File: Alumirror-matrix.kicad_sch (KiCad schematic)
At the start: 41 parts, among them K11 PG1350, K12 PG1350, K13 PG1350, K14 PG1350, K15 PG1350, K16 PG1350, K21 PG1350, K22 PG1350, K23 PG1350, K24 PG1350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

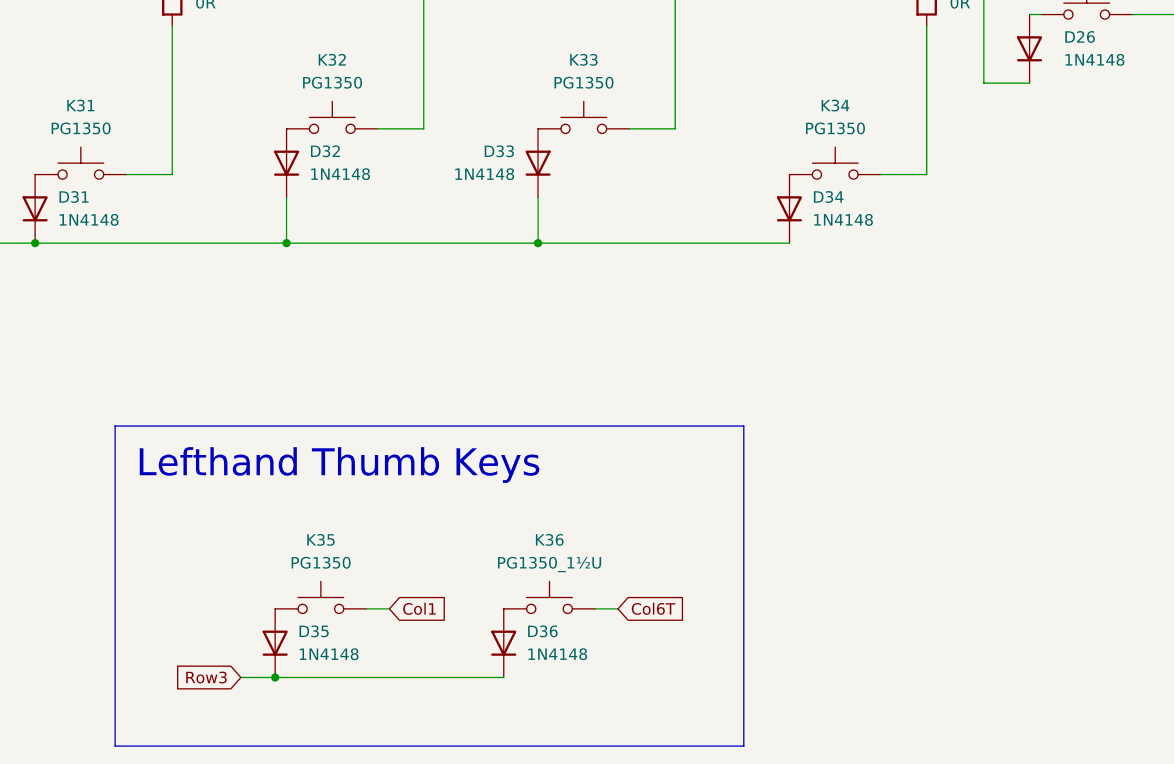
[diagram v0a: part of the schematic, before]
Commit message: Move thumb keys to new Row 4
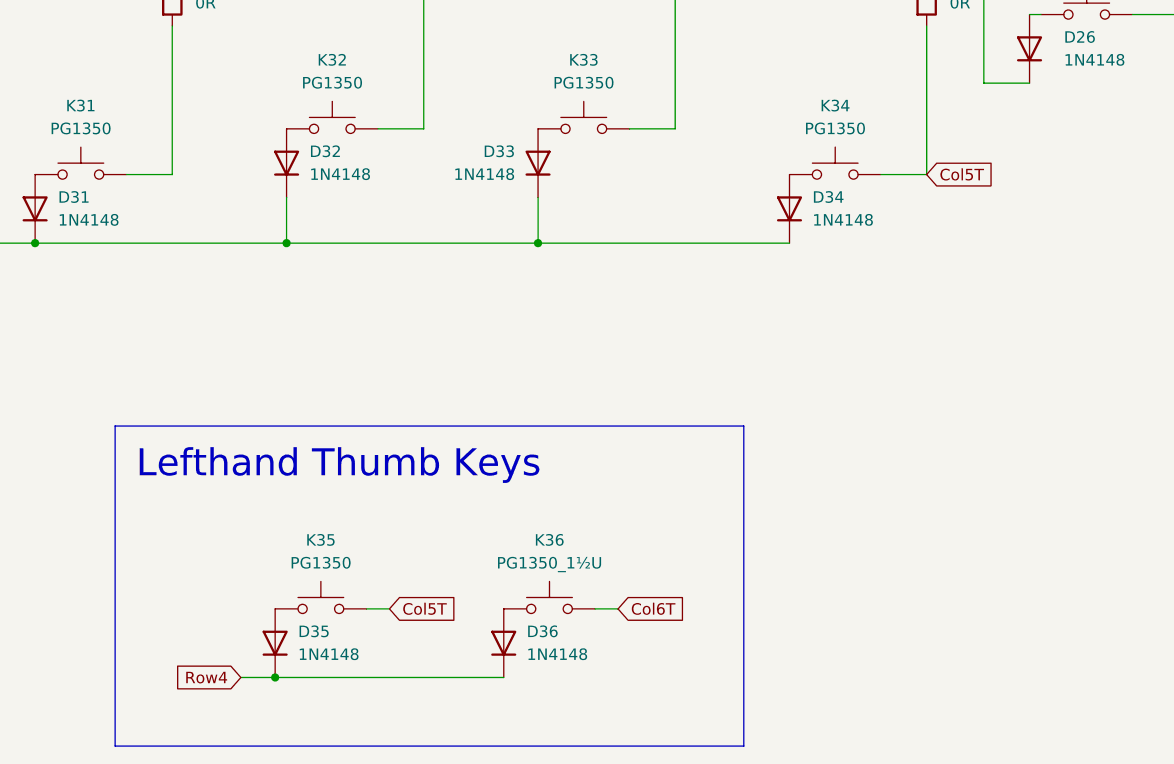
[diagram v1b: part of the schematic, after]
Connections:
- net Col1: no longer K35.1
- net Row3: no longer D35.1 (K), D36.1 (K)
- net Col5T: now reaches K34.1, R20.2
- net Col5T: now also K35.1
- new net Row4: D35.1 (K), D36.1 (K)
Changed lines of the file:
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@@
 		)
 	)
-	(global_label "Row3"
+	(global_label "Row4"
 		(shape input)
 		(at 123.19 154.94 180)
@@
 		)
 	)
-	(global_label "Col1"
+	(global_label "Col5T"
 		(shape input)
 		(at 139.7 147.32 0)
@@
 		)
 		(property "Intersheetrefs" "${INTERSHEET_REFS}"
-			(at 146.9789 147.32 0)
+			(at 147.9465 147.32 0)
 			(effects
 				(font
@@
 			(effects
 				(font
+					(size 1.27 1.27)
+				)
+				(justify left)
+				(hide yes)
+			)
+		)
+	)
+	(global_label "Col5T"
+		(shape input)
+		(at 199.39 99.06 0)
+		(fields_autoplaced yes)
+		(effects
+			(font
+				(size 1.27 1.27)
+			)
+			(justify left)
+		)
+		(property "Intersheetrefs" "${INTERSHEET_REFS}"
+			(at 207.6365 99.06 0)
+			(effects
+				(font
